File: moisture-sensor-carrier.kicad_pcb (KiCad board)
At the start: 4 copper layers, 34 x 155 mm, 58 parts, among them J1 USB-C receptacle, J2 Battery 503450 + NTC, J3 Solar panel, J4 SWD 10p 1.27mm, J5 Antenna feed, U1 nRF54L15-QFAA, U2 nPM1300-QEAA, U3 FDC1004, U4 SHT45-AD1F, X1 CM8V-T1A 32.768kHz CL=7pF 20p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, X2 32MHz CL=8pF 40ppm

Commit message: L1 = Murata LQM18PN4R7MFRL
Better than the TDK MLZ1608M4R7WT000, which met Nordic's numbers but sat
exactly on two of them. DCR 0.44 Ohm +/-25% gives 550 mOhm worst case
against the 650 mOhm limit, where the TDK's 0.5 +/-30% lands on 650
exactly.

Caveat recorded in BOM.md: the two current figures are not the same
measurement. TDK publishes a saturation current (120 mA at 50% L drop)
and a thermal one (350 mA); Murata's reference spec publishes only a
40 C temperature-rise rating of 620 mA and states no saturation current
at all. The Murata's headroom against Nordic's 120 mA is very likely much
better but this document does not confirm it - get the DC-bias curve from
the full datasheet or SimSurfing before volume.

Also noted: the document is stamped Reference Only, and DCR is not worth
optimising for power here - at a few mA the 100 mOhm difference is
microwatts against a wake cycle that is 0.6% of the budget. The reason to
prefer it is spec margin.

Co-Authored-By: Claude Opus 5 <noreply@anthropic.com>
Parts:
- L1: value 4.7uH 120mA 0603 -> LQM18PN4R7MFRL 4.7uH

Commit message: D5 = Panjit RB751V-40; X2 = Epson FA-128 8 pF
D5: 370 mV at 1 mA, 300 mA, 40 V reverse, 500 nA leakage, SOD-323,
$0.14. Chosen over BAT201M3, which has a lower drop (290 mV at 10 mA)
and 1 A rating but only 20 V reverse - thin against the 22 V VBUS abs max
that HARDWARE.md section 4 leans on - and 50 uA leakage. Recorded two
traps from the same search: RB751V-40WS and RB751V-40X share the 370 mV
figure but are rated 30 mA not 300, and BAS70WS/BAT42WS/BAT43WS all quote
1 V forward.

X2: 2016 was never a requirement, only Nordic's reference BOM. The
datasheet characterises 2.0x1.6 and 1.2x1.0 and mandates neither - the
small one passes at 100 ohm ESR because its C0 is 0.42 pF. C0 and ESR
trade on the Figure 17 curve; package size is a proxy.

FA-128 totals 25 ppm (12 initial + 12 temp over -20..+75 C + 1 aging)
against a 40 ppm requirement, where the ABM11A's best combination was 48.
ESR 60 ohm max at 32 MHz sits under the ~100 ohm the CL=8pF curve allows
at C0 0.74 pF. Two things to close: Epson does not publish C0, and their
recommended land pattern does not match KiCad's generic 2016 footprint -
the same mismatch that forced a vendor footprint for X1.

Co-Authored-By: Claude Opus 5 <noreply@anthropic.com>
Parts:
- D5: value OR-ing Schottky -> RB751V-40 Schottky
- X2: value 32MHz CL=8pF 40ppm -> FA-128 32MHz CL=8pF

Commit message: Cell = Adafruit 1578 (500 mAh); J2 = 2-pin JST PH
Cell drops from the 258 to the 1578 for fit margin. The 258 is 34.0 mm
across a 34.92 mm interior and its part code (503562) implies a 35 mm
nominal cell that would not go in at all; pouch cells also swell. 1578 is
29 mm across, 6 mm of slack, at a cost of 0.5 years (2.9 vs 3.45).

J2 becomes a 2-pin JST PH so an Adafruit cell plugs straight in. Drops the
pack-NTC pin, which costs nothing - Adafruit cells are 2-wire with no
thermistor, so the NTC path was always TH1.

PH is 8 mm against 6.90 mm of clearance under the cell, so tools_gen_pcb.py
now models the cell footprint and asserts that anything in COMPONENT_HEIGHTS
taller than the gap sits outside it. The cell covers 36 mm of the 74 mm
board, so the y 62-74 band keeps the full 11.70 mm and J2 goes there.

Power budget rescaled to 500 mAh. Worth noting the balance shifts: self
discharge falls from 92% of the budget on the 2000 mAh cell to 74% here,
and the PCM's quiescent current is now 16% - twice the whole nRF+PMIC
sleep draw. Measuring it matters more than it did.

Co-Authored-By: Claude Opus 5 <noreply@anthropic.com>
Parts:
- J2: value Battery 503450 + NTC -> Battery - Adafruit 1578; footprint JST_GH_SM03B-GHS-TB_1x03-1MP_P1.25mm_Horizontal -> JST_PH_B2B-PH-K_1x02_P2.00mm_Vertical
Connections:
- J2 pad 2: /NTC -> GND
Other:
- board text added: "CELL 29x36x4.8 ON LID - 6.90 mm CLEAR UNDER"

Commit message: SHT45 on a routed thermal island; move it out of the cell shadow
Sensirion's design guide section 3 says the dominant error path is
conduction through the PCB and the fix is milled slits around the sensor
(Figures 8b and 11b). U4 now sits on a peninsula formed by a C-shaped
1.0 mm routed slot, joined to the board by a single 2.8 mm neck. Not a
closed ring - the traces have to reach the pads, and Sensirion's own
figures show a neck.

This exposed a placement problem: U4 was at (30.0, 34.5), inside the cell
footprint. The cell is the largest thermal mass on the assembly and warms
while charging at 500 mA, so the sensor was sitting under the worst
possible thing. Moved to (29.5, 23.0) - 6.9 mm from U1, 32.1 mm from U2,
clear of the cell. Asserted in the generator both ways.

Split the keepout in two, because there were two different constraints
conflated into one. NoCopperSHT45 now covers only the strip under the die
between the pad columns and bans tracks/vias/pour, per datasheet 5.3.
SHT45_ThermalIsland covers the whole island and bans pour ONLY, per the
design guide. The old version sized the die keepout to the whole courtyard,
which would have banned the traces that have to reach the pads, and letting
ground flood the island both defeated the isolation and left an isolated
copper region DRC flagged.

Co-Authored-By: Claude Opus 5 <noreply@anthropic.com>
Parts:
- moved C27 15.1 mm to (85.8, 63.0)
- moved U4 11.5 mm to (89.5, 63.0)
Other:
- outline, holes or cut-outs redrawn

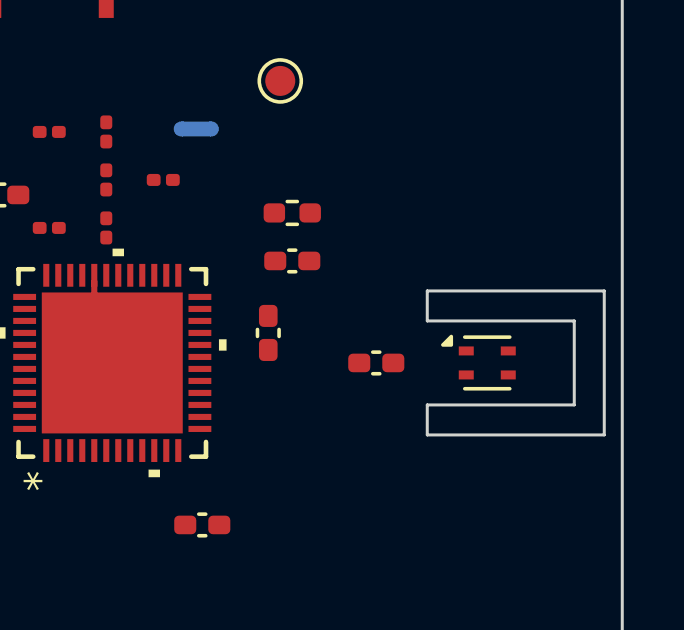
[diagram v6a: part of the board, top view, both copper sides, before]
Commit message: Circular SHT peninsula; fold in the corrected USB-C 3D orientation
The SHT45 island is now a 2.2 mm radius circle cut by an annular 1.0 mm
slot with a 60 degree opening, giving a 2.7 mm neck. Round rather than
rectangular: no stress-raising inside corners, and the island edge is a
smooth arc.

More importantly the slot now clears the board edge by 2.2 mm. The
rectangular version left 0.6 mm - a fragile sliver of FR4 exactly where
the box wall sits. The generator asserts a 2.0 mm minimum, and separately
that U4's furthest corner is inside the island radius and that the slot
does not encroach on the antenna keepout.

J1's 3D model orientation, corrected by hand in the viewer, is folded into
MODELS_3D: offset (0,-1,0) and rotation (-90,0,0). Without that the next
generator run would have silently overwritten it - the same Y-up CAD
convention as the SHT45, crystal and enclosure models.

Co-Authored-By: Claude Opus 5 <noreply@anthropic.com>
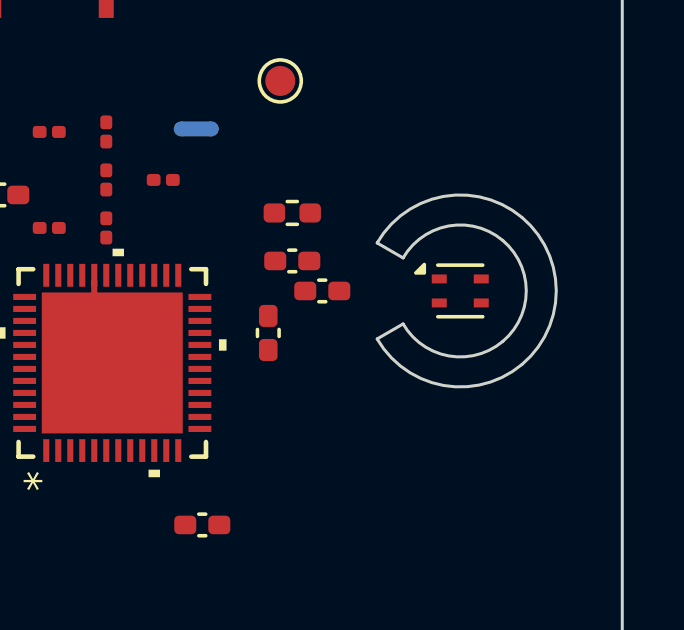
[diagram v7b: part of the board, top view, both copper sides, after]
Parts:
- moved C27 3.00 mm to (84.0, 60.6)
- moved U4 2.56 mm to (88.6, 60.6)
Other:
- outline, holes or cut-outs redrawn

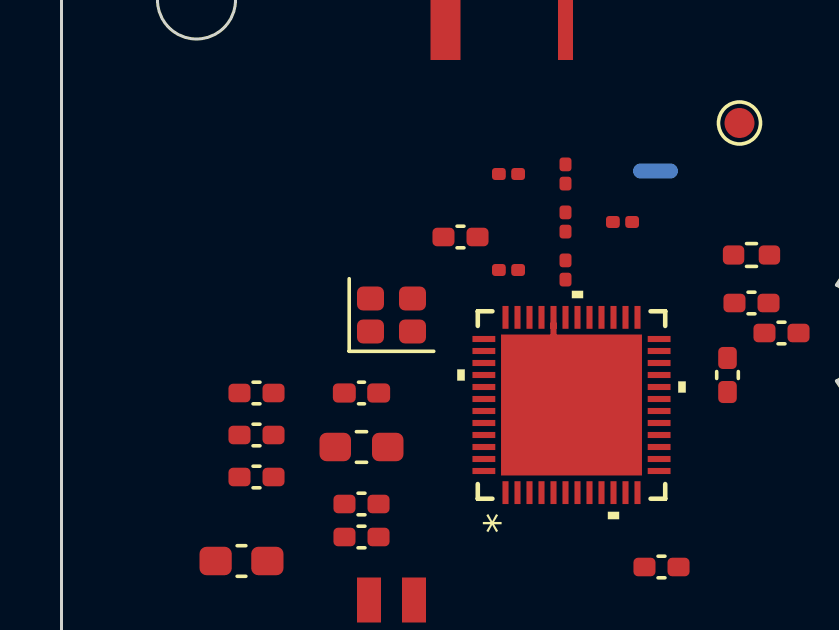
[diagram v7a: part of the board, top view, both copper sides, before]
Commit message: X2 land pattern; split the enclosure model into lid/bottom/gasket
X2 moves to an Epson-specific footprint. Their recommended land is
0.50 x 0.85 mm pads on 0.95 (X) by 1.15 (Y) centres, a 1.45 x 2.00 mm
envelope. KiCad's generic Crystal_SMD_2016-4Pin uses 0.90 x 0.80 pads on
1.40 x 1.10 centres - a 2.30 mm outer span, 0.85 mm wider than Epson
specify. Pads 1/3 are the crystal terminals, 2/4 the metal cover to
ground, matching the existing netlist.

Hammond ship the 1551WK as a STEP assembly, not one solid. Split with
OCCT into Bottom, Lid and Gasket, each with its own show flag, positions
preserved from the assembly:
  Bottom  y  0.00 - 16.91
  Lid     y 16.00 - 22.00
  Gasket  y 16.42 - 17.62

Those numbers answer the question directly: the PCB is not sandwiched
between the halves and is not the gasket. It sits on 4.00 mm posts inside
the bottom, top face at y = 5.60, about 11 mm below the gasket seam. The
seal is a separate silicone part.

Caveat: the split files are valid STEP with correct geometry, but
kicad-cli's renderer will not draw them while it does draw Hammond's
combined .stp. ENCL_SPLIT = False falls back to the combined model.

Co-Authored-By: Claude Opus 5 <noreply@anthropic.com>
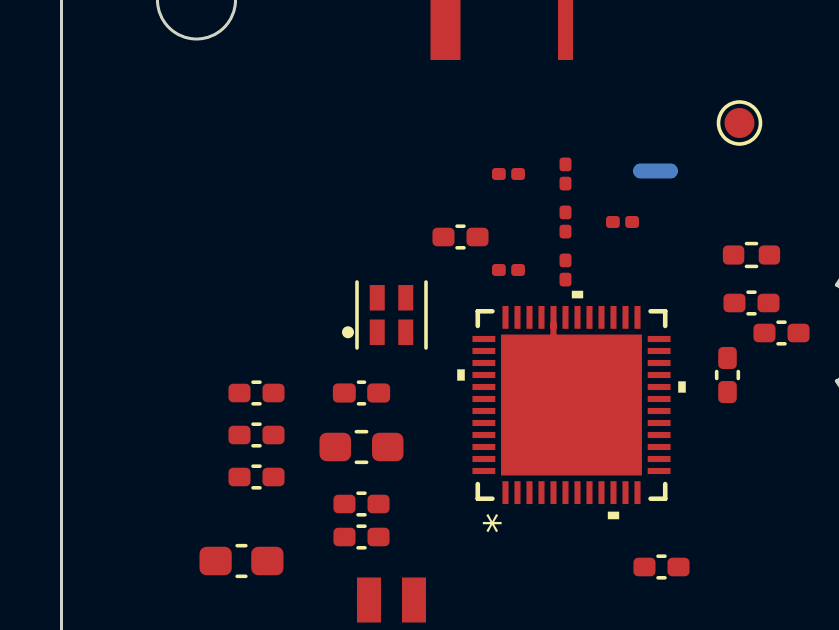
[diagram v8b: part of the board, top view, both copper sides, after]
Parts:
- added MP2, MP3: Hammond_1551WKBK, Enclosure_1551WK, F.Cu at (77.0, 77.0)
- X2: footprint Crystal_SMD_2016-4Pin_2.0x1.6mm -> XTAL_FA-128_2016_4Pin
